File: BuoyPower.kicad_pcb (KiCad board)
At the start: 2 copper layers, 56 x 65.5 mm, 38 parts, among them J1 Pololu-3782, J10 Conn_02x20_Odd_Even, J2 Conn_01x05, J4 Conn_01x02_Male, J5 Conn_01x03, J6 Conn_01x04, J7 Conn_01x02_Male, J8 Conn_01x04, J9 Conn_01x02_Male, Q1 IRLML2502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

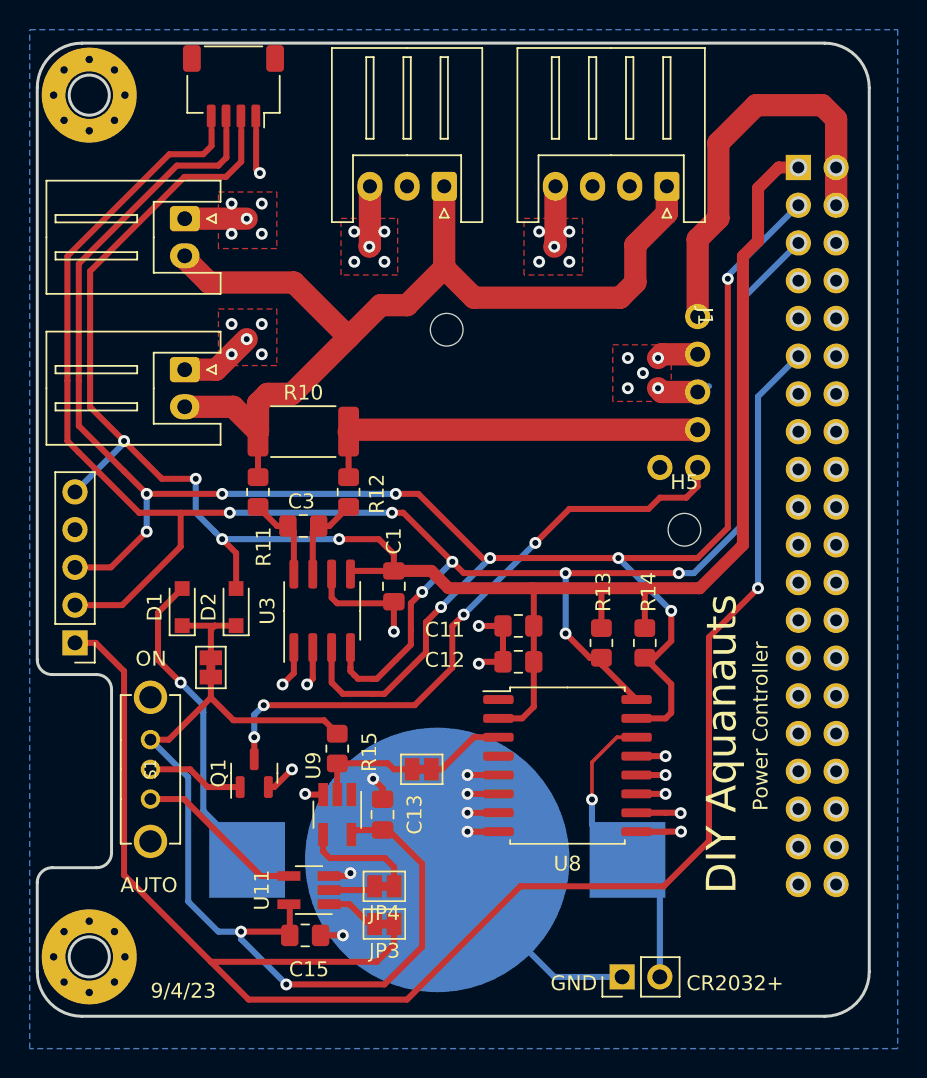
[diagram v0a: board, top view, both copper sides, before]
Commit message: revert to single layer
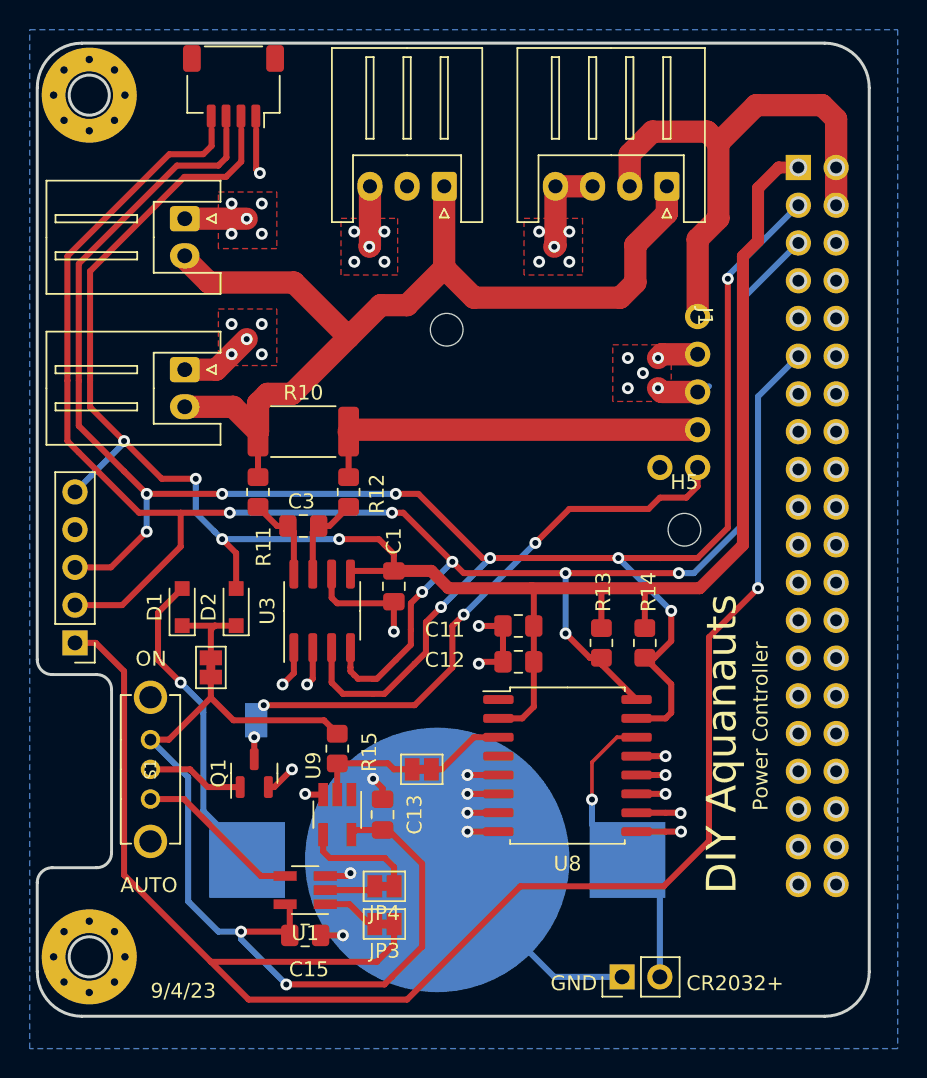
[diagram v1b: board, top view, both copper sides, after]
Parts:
- removed U11: SN74AHC1G32, Package_TO_SOT_SMD:SOT-23-5_HandSoldering
- added JP42: SolderJumper_2_Bridged, Jumper:SolderJumper-2_P1.3mm_Bridged_Pad1.0x1.5mm, B.Cu at (139.7, 111.3)
- added U1: 74AHC1G02, Package_TO_SOT_SMD:SOT-23-5_HandSoldering, F.Cu at (143.0, 122.7)
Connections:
- J8 pad 2: unconnected-(J8-Pin_2) -> +5V
- J8 pad 3: unconnected-(J8-Pin_3) -> GND
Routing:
- net +5V: track 27.4 -> 36.5 mm
- net GND: track 90.6 -> 93.1 mm

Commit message: Update readme
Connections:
- S1 pad 1: VCC -> GND
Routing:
- net VCC: track 64.9 -> 62.2 mm, vias 2 -> 3
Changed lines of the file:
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@@
       (stroke (width 0.127) (type solid)) (layer "F.Fab"))
     (pad "1" thru_hole circle locked (at -2 0 270) (size 1.308 1.308) (drill 0.8) (layers *.Cu *.Mask)
-      (net 55 "VCC") (pintype "passive") (solder_mask_margin 0.102))
+      (net 1 "GND") (pintype "passive") (solder_mask_margin 0.102))
     (pad "2" thru_hole circle locked (at 0 0 270) (size 1.308 1.308) (drill 0.8) (layers *.Cu *.Mask)
       (net 20 "Net-(Q1-G)") (pintype "passive") (solder_mask_margin 0.102))
@@
   (segment (start 150.876 120.904) (end 150.876 126.492) (width 0.4064) (layer "F.Cu") (net 55))
   (segment (start 148.6115 118.6395) (end 150.876 120.904) (width 0.4064) (layer "F.Cu") (net 55))
+  (segment (start 135 112) (end 136.652 110.348) (width 0.4064) (layer "F.Cu") (net 55))
   (segment (start 141.9645 123.6905) (end 141.906 123.632) (width 0.4064) (layer "F.Cu") (net 55))
   (segment (start 138.176 111.252) (end 136.652 109.728) (width 0.4064) (layer "F.Cu") (net 55))
@@
   (segment (start 141.9645 125.73) (end 141.9645 123.6905) (width 0.4064) (layer "F.Cu") (net 55))
   (segment (start 148.844 128.524) (end 148.336 129.032) (width 0.4064) (layer "F.Cu") (net 55))
+  (segment (start 136.652 110.348) (end 136.652 109.728) (width 0.4064) (layer "F.Cu") (net 55))
   (segment (start 144.272 111.252) (end 138.176 111.252) (width 0.4064) (layer "F.Cu") (net 55))
-  (segment (start 136.652 109.728) (end 133.826 112.554) (width 0.4064) (layer "F.Cu") (net 55))
   (segment (start 136.652 108.346) (end 136.652 109.728) (width 0.4064) (layer "F.Cu") (net 55))
   (segment (start 141.9645 126.2165) (end 141.9645 125.73) (width 0.4064) (layer "F.Cu") (net 55))
   (segment (start 148.209 118.6395) (end 146.4235 118.6395) (width 0.4064) (layer "F.Cu") (net 55))
   (segment (start 145.161 112.141) (end 144.272 111.252) (width 0.4064) (layer "F.Cu") (net 55))
-  (segment (start 133.826 112.554) (end 132.588 112.554) (width 0.4064) (layer "F.Cu") (net 55))
   (segment (start 145.1618 112.1562) (end 145.161 112.157) (width 0.4064) (layer "F.Cu") (net 55))
   (segment (start 145.161 112.157) (end 145.161 112.141) (width 0.4064) (layer "F.Cu") (net 55))
@@
   (via (at 138.684 125.476) (size 0.8) (drill 0.4) (layers "F.Cu" "B.Cu") (net 55))
   (via (at 141.732 129.032) (size 0.8) (drill 0.4) (layers "F.Cu" "B.Cu") (net 55))
+  (via (at 135 112) (size 0.8) (drill 0.4) (layers "F.Cu" "B.Cu") (net 55))
   (segment (start 141.732 129.032) (end 138.684 125.984) (width 0.4064) (layer "B.Cu") (net 55))
   (segment (start 135.128 123.444) (end 135.128 115.094) (width 0.4064) (layer "B.Cu") (net 55))
-  (segment (start 135.128 115.094) (end 132.588 112.554) (width 0.4064) (layer "B.Cu") (net 55))
+  (segment (start 135.128 112.128) (end 135 112) (width 0.4064) (layer "B.Cu") (net 55))
   (segment (start 137.16 125.476) (end 135.128 123.444) (width 0.4064) (layer "B.Cu") (net 55))
   (segment (start 138.684 125.476) (end 137.16 125.476) (width 0.4064) (layer "B.Cu") (net 55))
+  (segment (start 135.128 115.094) (end 135.128 112.128) (width 0.4064) (layer "B.Cu") (net 55))
   (segment (start 138.684 125.984) (end 138.684 125.476) (width 0.4064) (layer "B.Cu") (net 55))
   (segment (start 136.926 104.882) (end 138.3538 104.882) (width 0.4064) (layer "F.Cu") (net 56))
